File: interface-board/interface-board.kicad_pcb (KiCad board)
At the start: 2 copper layers, 182 x 110 mm, 98 parts, among them J1 HECS, J10 AUX, J11 UART, J12 NTC1, J13 NTC1, J14 RJ45, J15 ICSP, J2 CASEFAN1, J3 CASEFAN2, J4 AMPSEAL_PWR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

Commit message: Beginnings of board layout of interface-board
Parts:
- moved F3 236.3 mm to (-37.5, -37.8), turned to 90 degrees
- moved J14 161.0 mm to (-20.0, 31.5)
- moved C6 141.9 mm to (-22.0, 25.5), turned to 0 degrees
- moved C5 139.5 mm to (-26.0, 14.5), turned to 0 degrees
- moved Y1 130.6 mm to (-27.0, 19.0)
- moved J2 129.0 mm to (22.0, -56.5), turned to 90 degrees
- moved R4 128.0 mm to (-20.5, -30.0)
- moved RV1 127.8 mm to (73.0, 3.00)
- moved U2 126.0 mm to (-19.9, 19.4)
- moved C4 123.7 mm to (-15.0, 19.5), turned to 270 degrees
- moved R3 123.6 mm to (-15.0, 16.0)
- moved C3 123.4 mm to (-18.0, 15.0), turned to 180 degrees
- moved U1 122.5 mm to (-11.2, 19.3), turned to 270 degrees
- moved R1 119.5 mm to (-13.0, 24.5), turned to 180 degrees
- moved R2 115.8 mm to (-10.0, 24.5), turned to 180 degrees
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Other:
- rule trace_min: 0.2 -> 0.1524

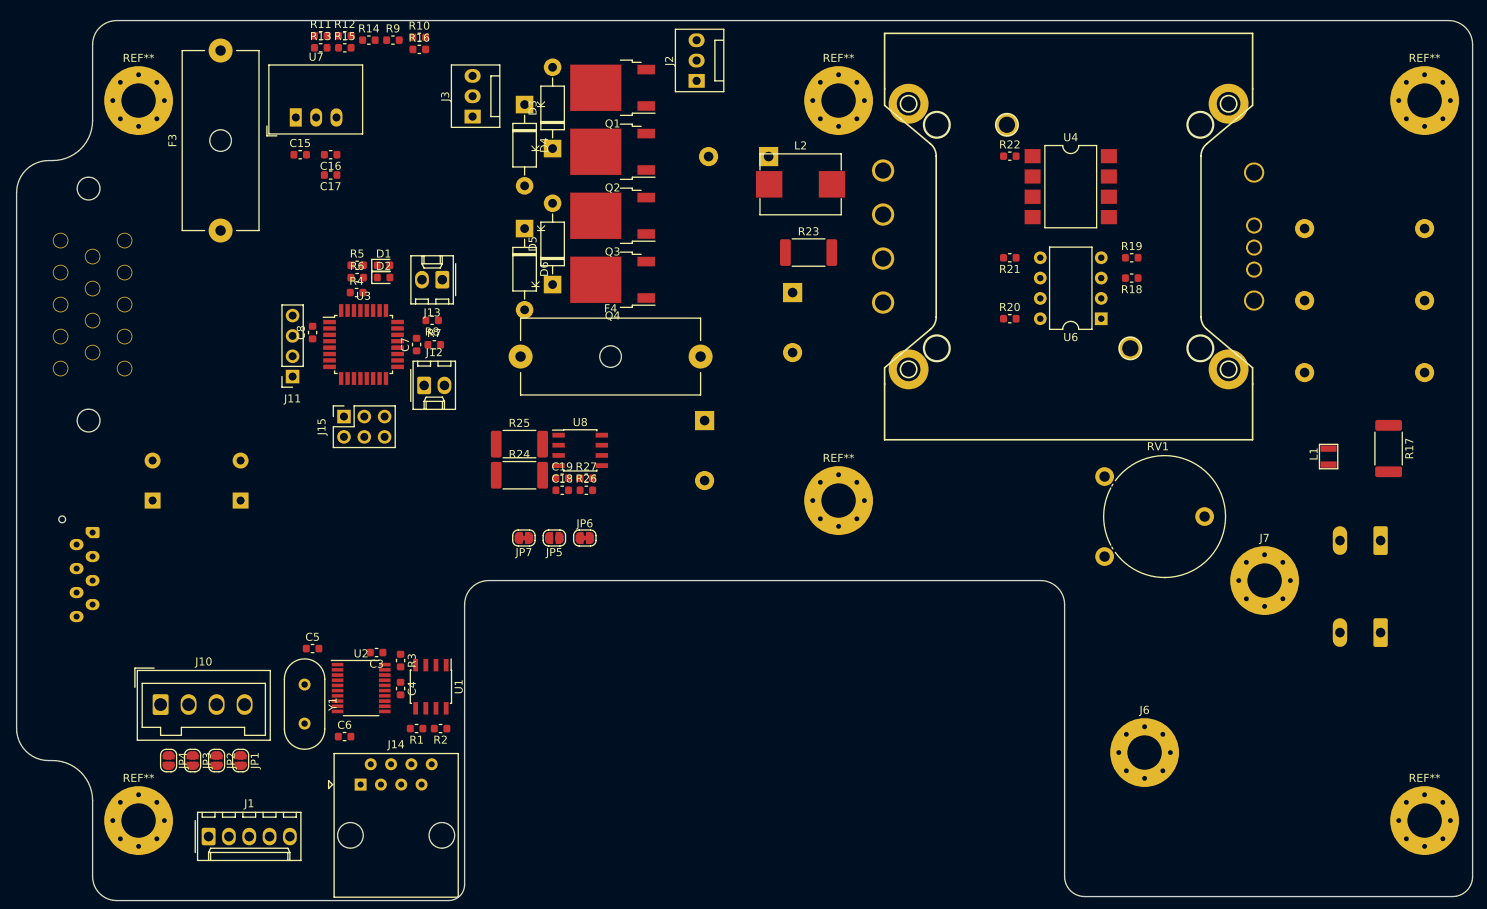
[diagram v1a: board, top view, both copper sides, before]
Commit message: Updated main connector and pinout
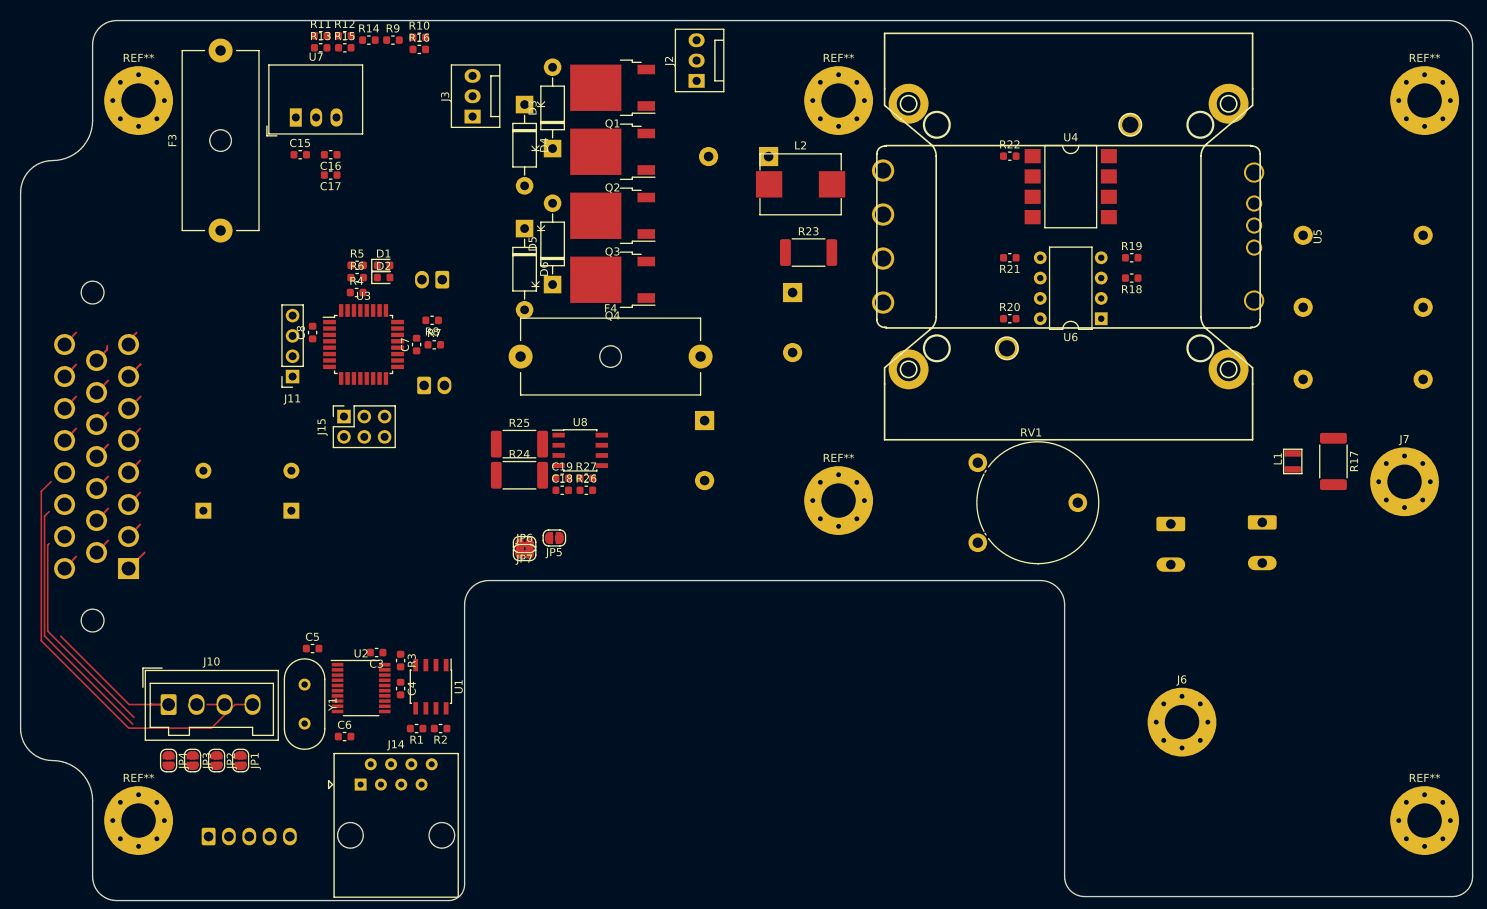
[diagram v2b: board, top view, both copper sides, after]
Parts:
- removed J4: AMPSEAL_PWR, Connector_JST:JST_ZE_B08B-ZESK-1D_1x08_P1.50mm_Vertical
- removed J5: AMPSEAL_MAIN, CustomFootprints:AMPSEAL 776266-1 14-PIN
- added J16: Conn_01x23, CustomFootprints:TE_1-776087-1, B.Cu at (-49.0, 4.50)
- J1, J12, J13: moved to B.Cu
- U5: footprint CustomFootprints:DCM4623TD2J13D0T70 w_landpattern -> CustomFootprints:DCM4623TD2J13D0T70_w_landpattern; moved to F.Cu
- moved J8 29.5 mm to (81.3, -1.07), turned to 270 degrees
- moved C11 24.2 mm to (97.8, -19.1), turned to 0 degrees
- moved C9 22.9 mm to (97.8, -37.1), turned to 0 degrees
- moved J7 21.4 mm to (110.5, -6.35)
- moved RV1 15.9 mm to (57.1, 1.27)
- moved C10 15.2 mm to (97.8, -28.1), turned to 0 degrees
- moved J9 15.0 mm to (92.7, -1.27), turned to 270 degrees
- moved JP6 7.75 mm to (0.50, 2.50)
- moved R17 7.09 mm to (101.6, -8.89)
- moved C1 6.48 mm to (-28.6, -2.73)
- moved C2 6.48 mm to (-39.6, -2.73)
- moved J6 6.03 mm to (82.7, 23.7)
- moved L1 4.52 mm to (96.5, -8.89)
- moved J10 1.00 mm to (-44.0, 21.5)
- moved JP7 0.82 mm to (0.50, 1.50)
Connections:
- J10 pad 4: Net-(J10-Pad4) -> (no net)
- JP1 pad 1: Net-(J10-Pad4) -> (no net)
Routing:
- net (no net): track 0.00 -> 51.5 mm
- net Net-(J10-Pad3): track 0.00 -> 32.6 mm
- net Net-(J10-Pad2): track 0.00 -> 26.5 mm
- net Net-(J10-Pad1): track 0.00 -> 17.2 mm
- net /SHDN_LOOP_OUT: track 0.00 -> 11.0 mm
- net GND: track 0.00 -> 8.17 mm
- net +12V: track 0.00 -> 4.13 mm
- net /FANOUT2: track 0.00 -> 2.31 mm
- net /FANOUT3: track 0.00 -> 2.09 mm
- net /IMD_AN3: track 0.00 -> 2.04 mm
- net /IMD_AN2: track 0.00 -> 2.04 mm
- net /IMD_AN1: track 0.00 -> 2.04 mm
- net /CAN-: track 0.00 -> 2.04 mm
- net /CAN+: track 0.00 -> 2.04 mm
- net +5V: track 0.00 -> 2.04 mm
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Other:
- board size 182 x 110 mm -> 181.5 x 110 mm

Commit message: Added IMD LV connector
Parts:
- removed J14: RJ45, Connector_RJ:RJ45_Amphenol_54602-x08_Horizontal
- added J4: Bender-LV, Connector_Molex:Molex_KK-254_AE-6410-05A_1x05_P2.54mm_Vertical, B.Cu at (-23.6, 38.5)
- U5: footprint CustomFootprints:DCM4623TD2J13D0T70_w_landpattern -> CustomFootprints:DCM4623TD2J13D0T70 w_landpattern
- moved J1 0.49 mm to (-38.9, 38.5)

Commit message: Fixed more shit
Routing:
- net (no net): track 51.5 -> 0.00 mm
- net Net-(J10-Pad3): track 32.6 -> 0.00 mm
- net Net-(J10-Pad2): track 26.5 -> 0.00 mm
- net Net-(J10-Pad1): track 17.2 -> 0.00 mm
- net /SHDN_LOOP_OUT: track 11.0 -> 0.00 mm
- net GND: track 8.17 -> 0.00 mm
- net +12V: track 4.13 -> 0.00 mm
- net /FANOUT2: track 2.31 -> 0.00 mm
- net /FANOUT3: track 2.09 -> 0.00 mm
- net /IMD_AN3: track 2.04 -> 0.00 mm
- net /IMD_AN2: track 2.04 -> 0.00 mm
- net /IMD_AN1: track 2.04 -> 0.00 mm
- net /CAN-: track 2.04 -> 0.00 mm
- net /CAN+: track 2.04 -> 0.00 mm
- net +5V: track 2.04 -> 0.00 mm
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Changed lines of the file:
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@@
-(kicad_pcb (version 20171130) (host pcbnew "(5.0.0)")
+(kicad_pcb (version 20171130) (host pcbnew "(5.0.2)-1")
   (general
     (thickness 1.6)
     (drawings 60)
-    (tracks 43)
+    (tracks 0)
     (zones 0)
     (modules 97)
@@
   (gr_line (start 119 -61) (end 119 43) (layer Edge.Cuts) (width 0.15))
   (gr_line (start 116 -64) (end -50.5 -64) (layer Edge.Cuts) (width 0.15))
-  (segment (start -35.7032 21.5) (end -38.6482 24.445) (width 0.2032) (layer F.Cu) (net 0))
-  (segment (start -34.5 21.5) (end -35.7032 21.5) (width 0.2032) (layer F.Cu) (net 0) (status 10))
-  (segment (start -38.6482 24.445) (end -48.99 24.445) (width 0.2032) (layer F.Cu) (net 0))
-  (segment (start -59.910522 13.524478) (end -59.910522 -5.134478) (width 0.2032) (layer F.Cu) (net 0))
-  (segment (start -48.99 24.445) (end -59.910522 13.524478) (width 0.2032) (layer F.Cu) (net 0))
-  (segment (start -59.910522 -5.134478) (end -58.684435 -6.360565) (width 0.2032) (layer F.Cu) (net 0))
-  (segment (start -48.99 -15.555) (end -48.945 -15.555) (width 0.25) (layer F.Cu) (net 1) (status 30))
-  (segment (start -48.945 -15.555) (end -47.5 -17) (width 0.25) (layer F.Cu) (net 1) (status 10))
-  (segment (start -52.99 -17.555) (end -51.545 -19) (width 0.25) (layer F.Cu) (net 1) (status 10))
-  (segment (start -48.99 -3.555) (end -47.545 -5) (width 0.25) (layer F.Cu) (net 2) (status 10))
-  (segment (start -48.99 -7.555) (end -47.545 -9) (width 0.25) (layer F.Cu) (net 2) (status 10))
-  (segment (start -48.99 -11.555) (end -47.545 -13) (width 0.25) (layer F.Cu) (net 2) (status 10))
-  (segment (start -52.99 -13.555) (end -51.545 -15) (width 0.25) (layer F.Cu) (net 2) (status 10))
-  (segment (start -56.99 -23.555) (end -55.545 -25) (width 0.25) (layer F.Cu) (net 3) (status 10))
-  (segment (start -51.677501 -22.867499) (end -51.677501 -23.322499) (width 0.25) (layer F.Cu) (net 18))
-  (segment (start -52.99 -21.555) (end -51.677501 -22.867499) (width 0.25) (layer F.Cu) (net 18) (status 10))
-  (segment (start -48.99 -23.555) (end -48.99 -24.01) (width 0.25) (layer F.Cu) (net 19) (status 30))
-  (segment (start -48.99 -24.01) (end -48 -25) (width 0.25) (layer F.Cu) (net 19) (status 10))
-  (segment (start -48.99 -19.555) (end -47.545 -21) (width 0.25) (layer F.Cu) (net 20) (status 10))
-  (segment (start -47.545 -21) (end -47.5 -21) (width 0.25) (layer F.Cu) (net 20))
-  (segment (start -56.99 -19.555) (end -55.545 -21) (width 0.25) (layer F.Cu) (net 23) (status 10))
-  (segment (start -56.99 -15.555) (end -55.545 -17) (width 0.25) (layer F.Cu) (net 24) (status 10))
-  (segment (start -56.99 -11.555) (end -55.545 -13) (width 0.25) (layer F.Cu) (net 25) (status 10))
-  (segment (start -46.1 21.5) (end -46.155 21.445) (width 0.25) (layer F.Cu) (net 26))
-  (segment (start -45 21.5) (end -46.1 21.5) (width 0.25) (layer F.Cu) (net 26) (status 10))
-  (segment (start -45 21.5) (end -48.935 21.5) (width 0.2032) (layer F.Cu) (net 26) (status 10))
-  (segment (start -48.935 21.5) (end -57.49 12.945) (width 0.2032) (layer F.Cu) (net 26))
-  (segment (start -41.5 21.5) (end -41.5 21.8) (width 0.2032) (layer F.Cu) (net 27) (status 30))
-  (segment (start -59.104101 12.330899) (end -59.104101 1.559101) (width 0.2032) (layer F.Cu) (net 27))
-  (segment (start -48.33339 23.10161) (end -59.104101 12.330899) (width 0.2032) (layer F.Cu) (net 27))
-  (segment (start -59.104101 1.559101) (end -58.934435 1.389435) (width 0.2032) (layer F.Cu) (net 27))
-  (segment (start -38 21.5) (end -39.2032 21.5) (width 0.2032) (layer F.Cu) (net 28) (status 10))
-  (segment (start -59.507316 12.927683) (end -59.507316 -2.037684) (width 0.2032) (layer F.Cu) (net 28))
-  (segment (start -48.49 23.945) (end -59.507316 12.927683) (width 0.2032) (layer F.Cu) (net 28))
-  (segment (start -59.507316 -2.037684) (end -58.934435 -2.610565) (width 0.2032) (layer F.Cu) (net 28))
-  (segment (start -52.99 -9.555) (end -51.545 -11) (width 0.25) (layer F.Cu) (net 29) (status 10))
-  (segment (start -52.99 -5.555) (end -51.545 -7) (width 0.25) (layer F.Cu) (net 30) (status 10))
-  (segment (start -56.99 4.445) (end -55.545 3) (width 0.25) (layer F.Cu) (net 39) (status 10))
-  (segment (start -52.99 2.445) (end -51.545 1) (width 0.25) (layer F.Cu) (net 39) (status 10))
-  (segment (start -48.99 4.445) (end -48.945 4.445) (width 0.25) (layer F.Cu) (net 39) (status 30))
-  (segment (start -48.945 4.445) (end -47 2.5) (width 0.25) (layer F.Cu) (net 39) (status 10))
-  (segment (start -48.99 0.445) (end -47.545 -1) (width 0.25) (layer F.Cu) (net 39) (status 10))
-  (segment (start -52.99 -1.555) (end -51.545 -3) (width 0.25) (layer F.Cu) (net 39) (status 10))
 )

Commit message: did some stuff
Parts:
- J6: footprint MountingHole:MountingHole_4.3mm_M4_Pad_Via -> MountingHole:MountingHole_6.4mm_M6_Pad_Via
- moved J6 17.0 mm to (99.0, 19.0)
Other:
- outline, holes or cut-outs redrawn

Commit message: updated test-board
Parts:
- U5: footprint CustomFootprints:DCM4623TD2J13D0T70 w_landpattern -> CustomFootprints:DCM4623TD2J13D0T70_w_landpattern-SP3

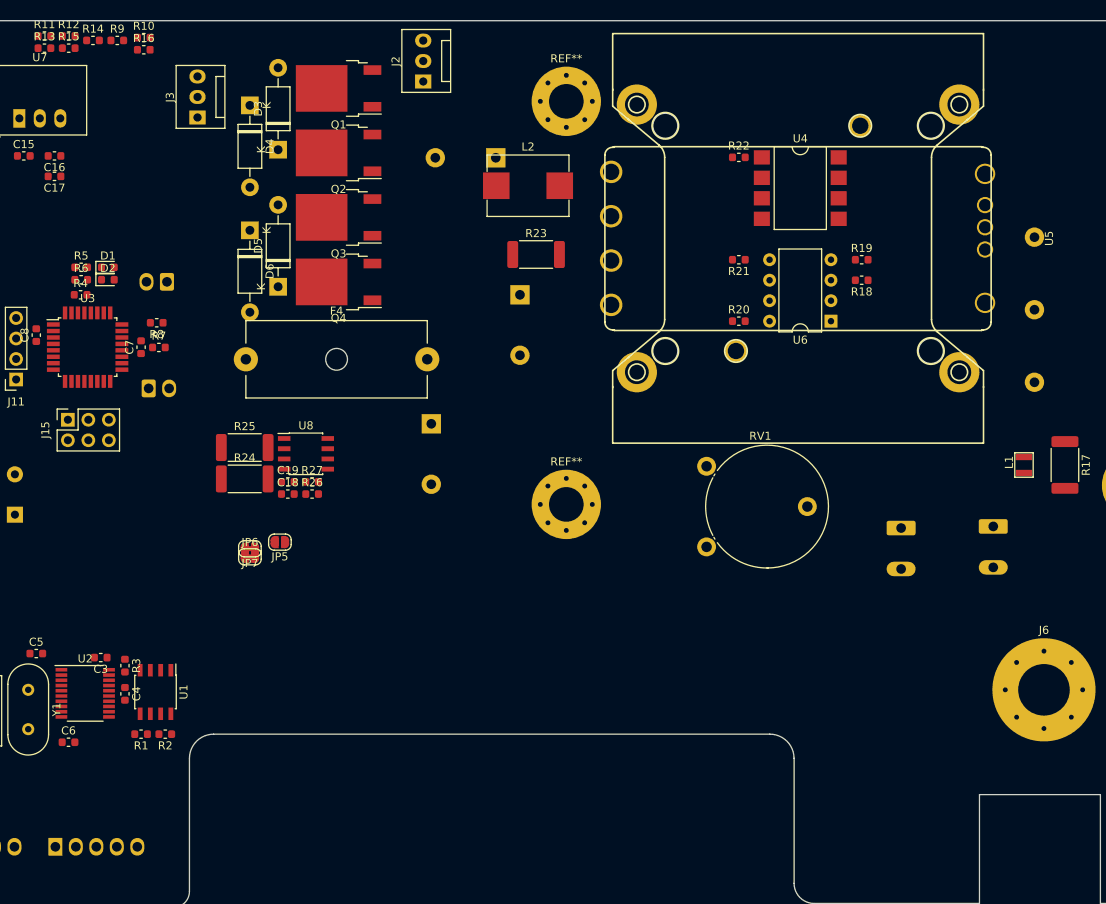
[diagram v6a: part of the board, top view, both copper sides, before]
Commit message: Footprints centralized now
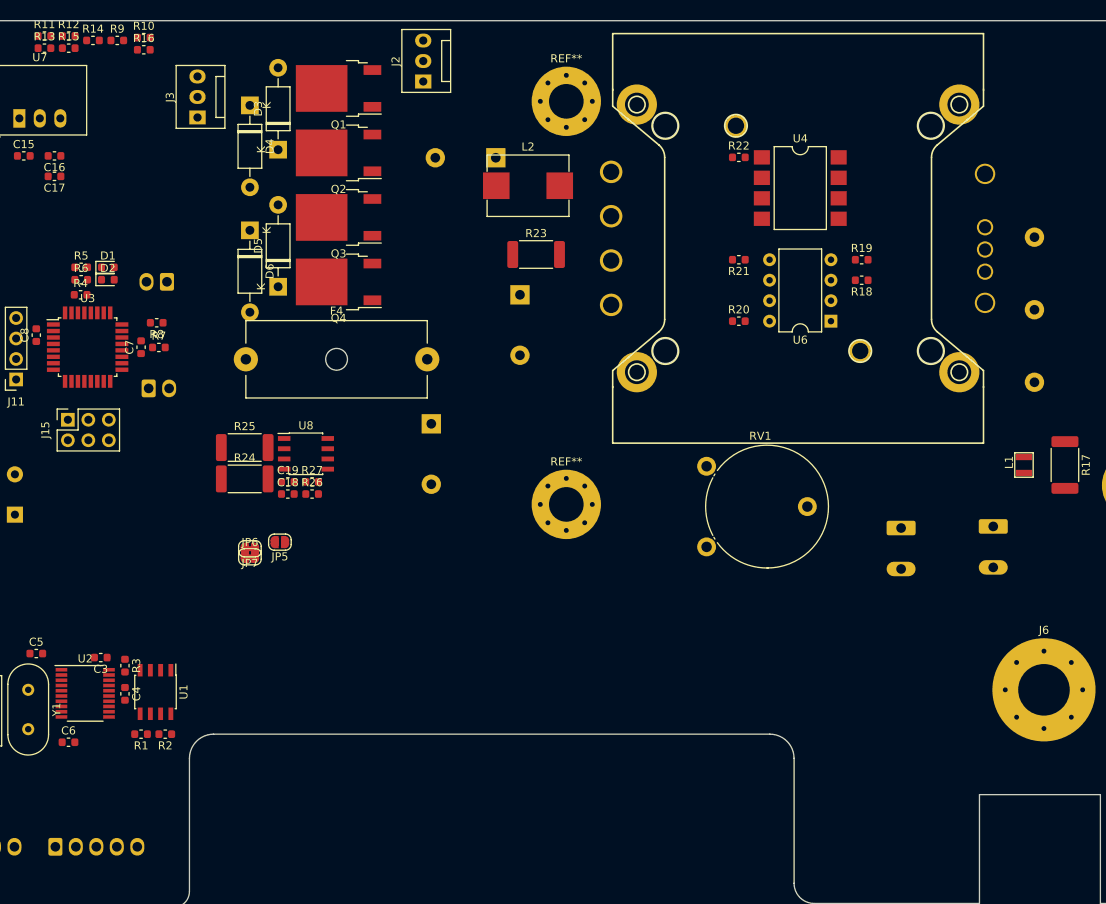
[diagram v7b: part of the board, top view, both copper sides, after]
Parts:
- U5: footprint CustomFootprints:DCM4623TD2J13D0T70_w_landpattern-SP3 -> CustomFootprints:DCM4623TD2J13D0T70_w_landpattern; moved to B.Cu

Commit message: Getting there with layout of big board...
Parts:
- removed F3: 1A, Fuse:Fuseholder_Cylinder-5x20mm_Schurter_0031_8201_Horizontal_Open
- removed F4: 20A, Fuse:Fuseholder_Cylinder-5x20mm_Schurter_0031_8201_Horizontal_Open
- removed JP1, JP4: Jumper, Jumper:SolderJumper-2_P1.3mm_Open_RoundedPad1.0x1.5mm
- removed JP5: SolderJumper_2_Open, Jumper:SolderJumper-2_P1.3mm_Open_RoundedPad1.0x1.5mm
- removed JP6, JP7: SolderJumper_2_Bridged, Jumper:SolderJumper-2_P1.3mm_Bridged_RoundedPad1.0x1.5mm
- removed R10, R11, R12, R13, R14, R15, R16, R9: R_US, Resistor_SMD:R_0603_1608Metric
- added F1: 2A, CustomFootprints:Fuseholder_Cylinder-5x20mm_Schurter_0031_8201_Horizontal_Open_3d, F.Cu at (112.4, 0.44)
- added RN1: 1k, Resistor_SMD:R_Array_Convex_4x0603, F.Cu at (12.0, -29.4)
- added RN2: 10k, Resistor_SMD:R_Array_Convex_4x0603, F.Cu at (8.24, -29.4)
- added U9: TLP184, CustomFootprints:TLP182, F.Cu at (70.5, -30.9)
- C15, J2, J3: moved to B.Cu
- J16: footprint CustomFootprints:TE_1-776087-1 -> 1-776087-1:TE_1-776087-1
- R18: value 50k -> 6.8k
- RV1: value 5k -> 50k; footprint Potentiometer_THT:Potentiometer_Piher_PT-15-V02_Vertical -> CustomFootprints:TC33X-503ECT-ND
- U4: value LTV-827S -> LTV-817S; footprint Package_DIP:SMDIP-8_W9.53mm -> Package_DIP:SMDIP-4_W9.53mm
- U6: value LTV-824 -> LTV-817S; footprint Package_DIP:DIP-8_W7.62mm -> Package_DIP:SMDIP-4_W9.53mm
- moved U7 68.7 mm to (-95.7, -39.6)
- moved C15 66.0 mm to (-93.4, -43.4)
- moved J7 65.7 mm to (48.9, 16.5)
- moved C16 57.9 mm to (-81.5, -43.8)
- moved C17 57.9 mm to (-81.5, -41.2)
- moved J2 52.4 mm to (-30.3, -53.1)
- moved JP2 51.6 mm to (-80.8, -0.26), turned to 0 degrees
- moved RV1 50.3 mm to (83.4, -41.6), turned to 90 degrees
- moved J10 47.9 mm to (-88.1, 2.82), turned to 90 degrees
- moved JP3 47.4 mm to (-80.8, 2.74), turned to 0 degrees
- moved D4 46.2 mm to (-44.9, -44.8), turned to 0 degrees
- moved C7 45.4 mm to (-18.1, 21.6)
- moved C8 45.4 mm to (-31.1, 20.1)
- moved D2 45.4 mm to (-22.2, 13.2)
- moved J11 45.4 mm to (-33.6, 25.6)
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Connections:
- C15 pad 1: /DC->DC Converters/12V_IN -> +12V
- J10 pad 3: Net-(J10-Pad3) -> (no net)
- J16 pad 17: Net-(J10-Pad3) -> Net-(J10-Pad2)
- J16 pad 18: Net-(J10-Pad2) -> Net-(J10-Pad1)
- J16 pad 19: Net-(J10-Pad1) -> /IMD_OK
- J16 pad 23: +5V -> (no net)
- J4 pad 4: (no net) -> /IMD_OK
- JP2 pad 1: Net-(J10-Pad3) -> Net-(J10-Pad2)
- JP3 pad 1: Net-(J10-Pad2) -> Net-(J10-Pad1)
- L1 pad 1: /HV+ -> /DC->DC Converters/HV+
- R17 pad 2: /HV+ -> /DC->DC Converters/HV+
- R18 pad 1: /DC->DC Converters/FAULT_HV -> Net-(R18-Pad1)
- R24 pad 1: /meter/OUT -> /SHDN_LOOP_OUT
- R24 pad 2: /meter/IN -> /DC->DC Converters/12V_OUT
- R25 pad 1: /meter/OUT -> /SHDN_LOOP_OUT
- R25 pad 2: /meter/IN -> /DC->DC Converters/12V_OUT
- R26 pad 2: /meter/IN -> /DC->DC Converters/12V_OUT
- R27 pad 2: /meter/OUT -> /SHDN_LOOP_OUT
- RV1 pad 2: /HV- -> Net-(R18-Pad1)
- U4 pad 3: (no net) -> /HV-
- U4 pad 4: (no net) -> /DC->DC Converters/TRIM_HV
- U6 pad 1: /DC->DC Converters/EN_HV -> Net-(R20-Pad2)
- U6 pad 2: /HV- -> GND
- U6 pad 4: Net-(R19-Pad1) -> /DC->DC Converters/EN_HV
- U7 pad 1: /DC->DC Converters/12V_IN -> +12V
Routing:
- net /HV-: track 0.00 -> 139.4 mm
- net /CAN-: track 0.00 -> 112.1 mm
- net /CAN+: track 0.00 -> 104.8 mm
- net /IMD_OK: track 0.00 -> 74.0 mm
- net /IMD_AN3: track 0.00 -> 70.2 mm
- net /IMD_AN2: track 0.00 -> 67.8 mm
- net /IMD_AN1: track 0.00 -> 64.3 mm
- net Net-(C10-Pad1): track 0.00 -> 55.8 mm
- net /HV+: track 0.00 -> 50.4 mm
- net /FANOUT3: track 0.00 -> 40.4 mm
- net /FANOUT2: track 0.00 -> 40.2 mm
- net /FANOUT1: track 0.00 -> 32.6 mm
- net /FANOUT0: track 0.00 -> 30.7 mm
- net /SHDN_LOOP_OUT: track 0.00 -> 30.5 mm
- net /DC->DC Converters/TRIM_HV: track 0.00 -> 22.9 mm
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- added copper zone on B.Cu, net +12V
- added copper zone on F.Cu, net /SHDN_LOOP_OUT
- added copper zone on F.Cu, net GND
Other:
- outline, holes or cut-outs redrawn
